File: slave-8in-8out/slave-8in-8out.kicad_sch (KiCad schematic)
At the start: 17 parts, among them J1 Conn_01x06_Male, J2 Screw_Terminal_01x02, J3 Conn_01x06_Female, J4 Screw_Terminal_01x04, J5 Screw_Terminal_01x04, J6 Screw_Terminal_01x04, J7 Screw_Terminal_01x04, J8 Conn_01x10_Male, J9 Screw_Terminal_01x02, SW1 SW_DIP_x03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

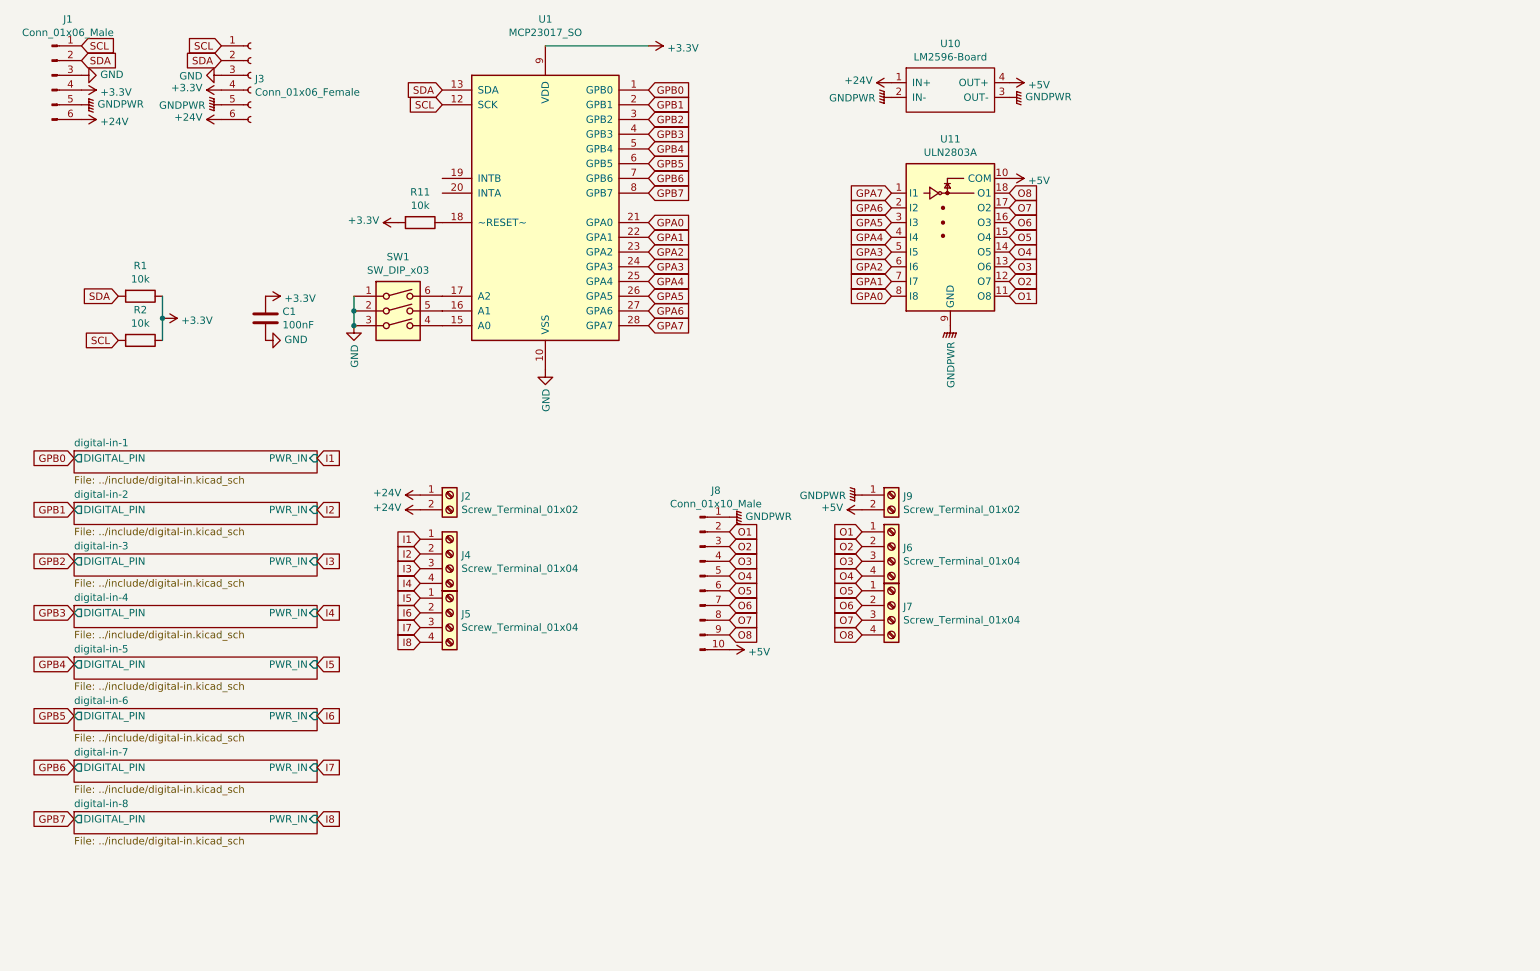
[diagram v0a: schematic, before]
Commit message: refactor 8in-8out
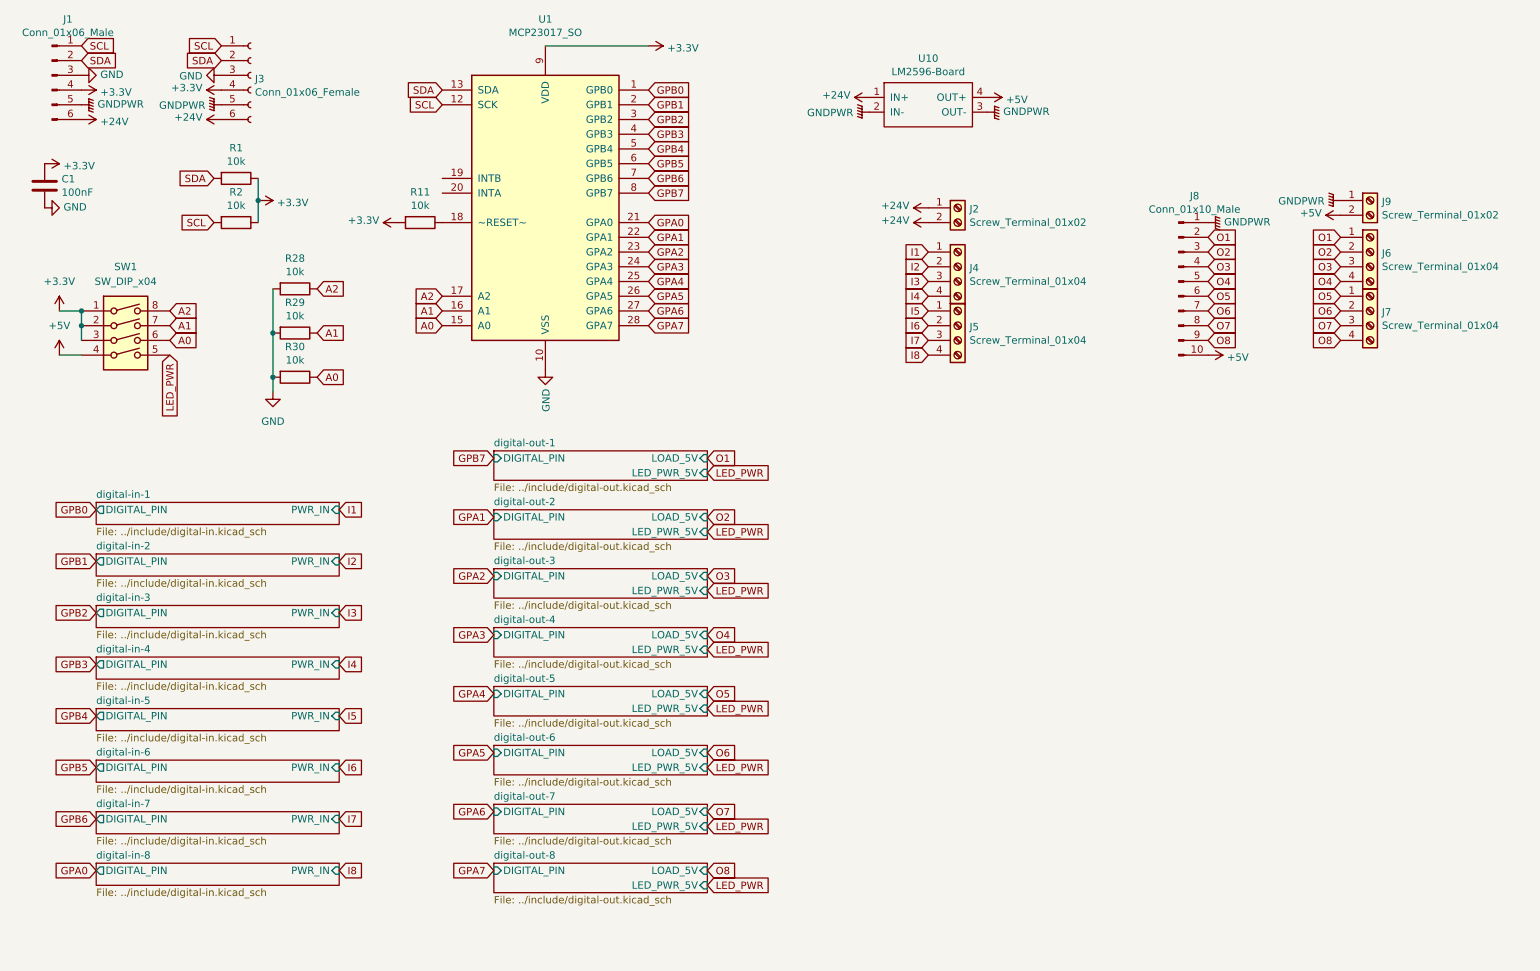
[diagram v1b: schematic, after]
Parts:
- removed SW1: SW_DIP_x03, Button_Switch_THT:SW_DIP_SPSTx03_Slide_9.78x9.8mm_W7.62mm_P2.54mm, symbol Switch:SW_DIP_x03
- removed U11: ULN2803A, Package_SO:SOIC-18W_7.5x11.6mm_P1.27mm, symbol Transistor_Array:ULN2803A
- added R28, R29, R30: 10k, Resistor_SMD:R_0402_1005Metric, symbol Device:R
- added SW1: SW_DIP_x04, Button_Switch_THT:SW_DIP_SPSTx04_Slide_9.78x12.34mm_W7.62mm_P2.54mm, symbol Switch:SW_DIP_x04
- R1, R11, R2: footprint Resistor_SMD:R_0805_2012Metric -> Resistor_SMD:R_0402_1005Metric; LCSC C17414 -> C25744
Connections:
- net +3V3: now also SW1.1, SW1.2, SW1.3
- net +5V: now also SW1.4
- net GND: now also R28.2, R29.2, R30.2
- net A0: now reaches U1.15 (A0)
- net A0: now also R30.1, SW1.6
- net A1: now reaches U1.16 (A1)
- net A1: now also R29.1, SW1.7
- net A2: now reaches U1.17 (A2)
- net A2: now also R28.1, SW1.8
- new net LED_PWR: SW1.5
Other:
- added sheet digital-out-1 (../include/digital-out.kicad_sch)
- added sheet digital-out-2 (../include/digital-out.kicad_sch)
- added sheet digital-out-3 (../include/digital-out.kicad_sch)
- added sheet digital-out-4 (../include/digital-out.kicad_sch)
- added sheet digital-out-5 (../include/digital-out.kicad_sch)
- added sheet digital-out-6 (../include/digital-out.kicad_sch)
- added sheet digital-out-7 (../include/digital-out.kicad_sch)
- added sheet digital-out-8 (../include/digital-out.kicad_sch)
- moved on the sheet: C1, J2, J4, J5, J6, J7, J8, J9, U10

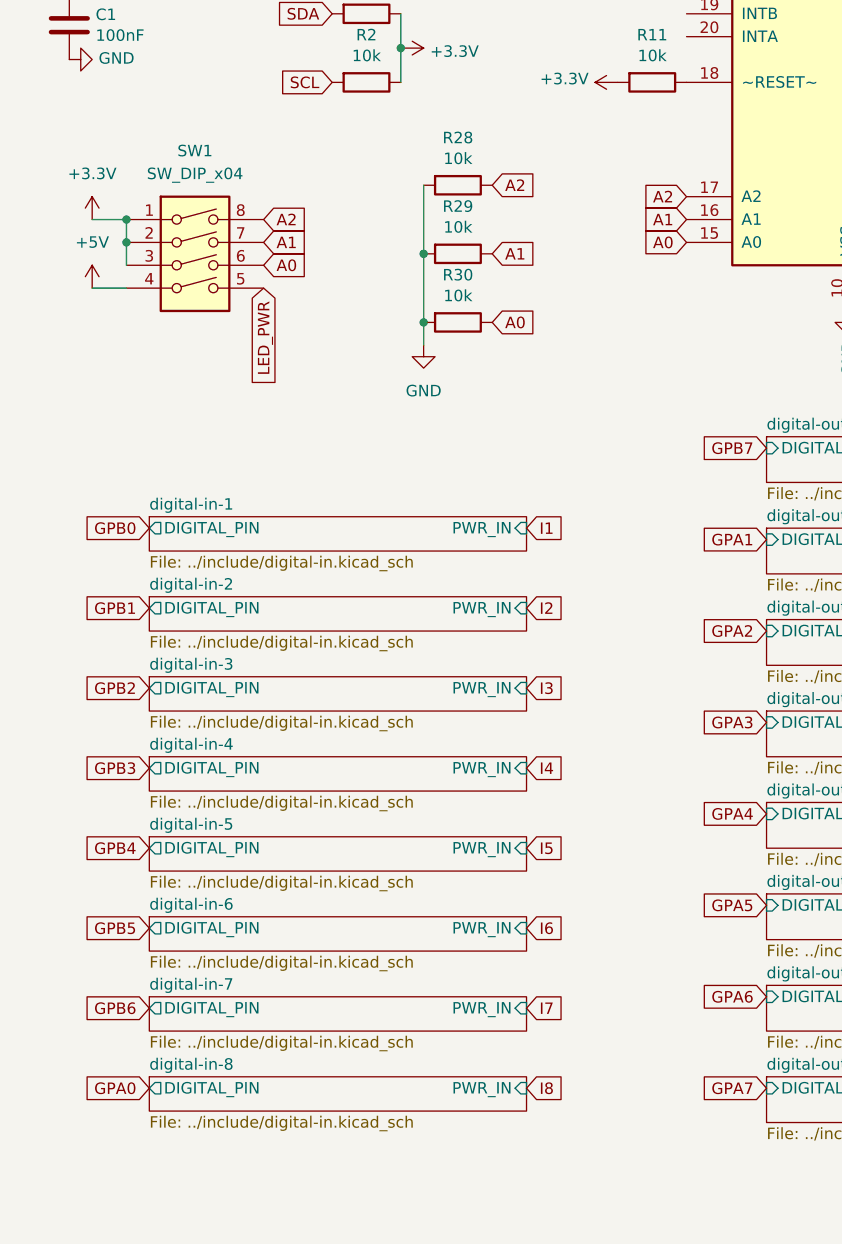
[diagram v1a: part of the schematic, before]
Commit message: refactor slave-8in-8out
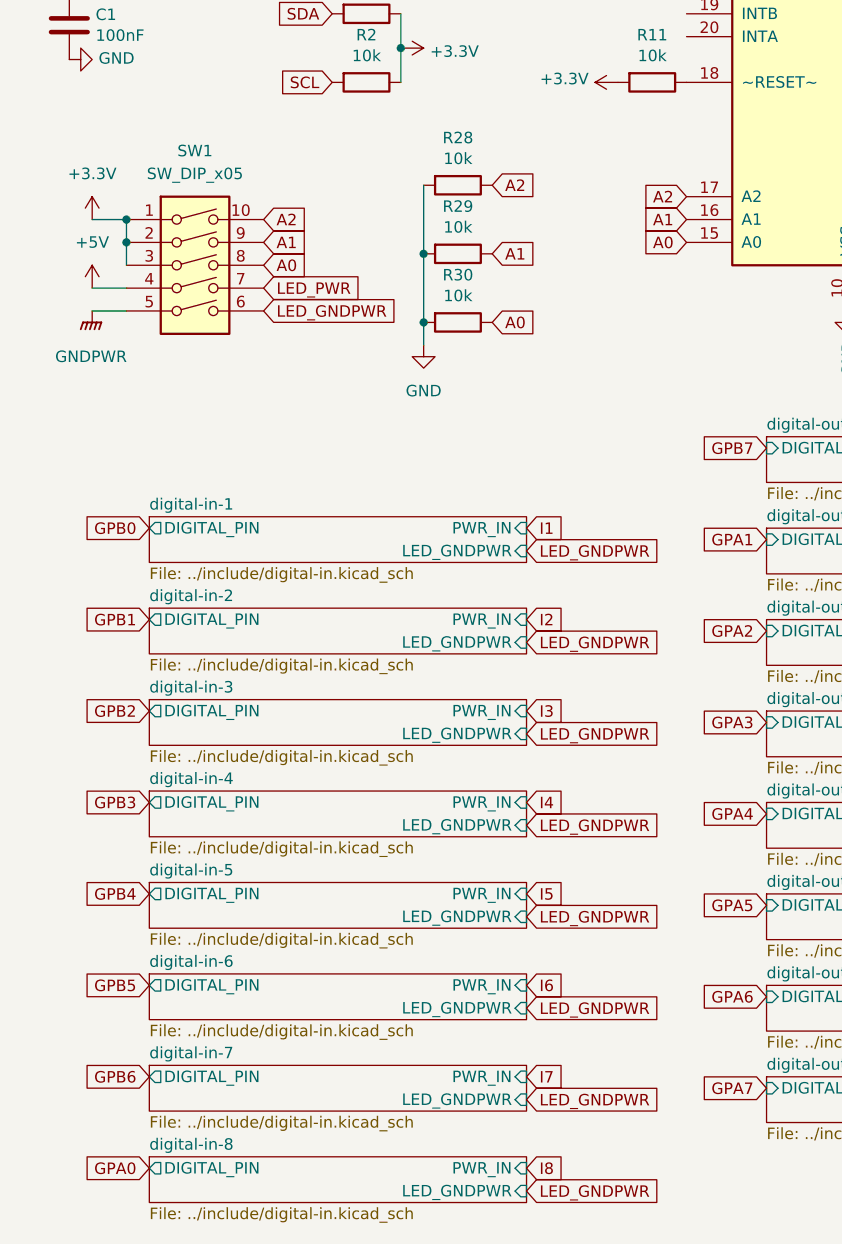
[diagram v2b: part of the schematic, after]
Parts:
- removed SW1: SW_DIP_x04, Button_Switch_THT:SW_DIP_SPSTx04_Slide_9.78x12.34mm_W7.62mm_P2.54mm, symbol Switch:SW_DIP_x04
- added SW1: SW_DIP_x05, Button_Switch_THT:SW_DIP_SPSTx05_Slide_9.78x14.88mm_W7.62mm_P2.54mm, symbol Switch:SW_DIP_x05
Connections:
- net +3V3: now also SW1.1, SW1.2, SW1.3
- net +5V: now also SW1.4
- net A0: now also SW1.8
- net A1: now also SW1.9
- net A2: now also SW1.10
- net GNDPWR: now also SW1.5
- net LED_PWR: now also SW1.7
- new net LED_GNDPWR: SW1.6
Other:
- sheet digital-in-1 ports: added LED_GNDPWR; removed none
- sheet digital-in-2 ports: added LED_GNDPWR; removed none
- sheet digital-in-3 ports: added LED_GNDPWR; removed none
- sheet digital-in-4 ports: added LED_GNDPWR; removed none
- sheet digital-in-5 ports: added LED_GNDPWR; removed none
- sheet digital-in-6 ports: added LED_GNDPWR; removed none
- sheet digital-in-7 ports: added LED_GNDPWR; removed none
- sheet digital-in-8 ports: added LED_GNDPWR; removed none

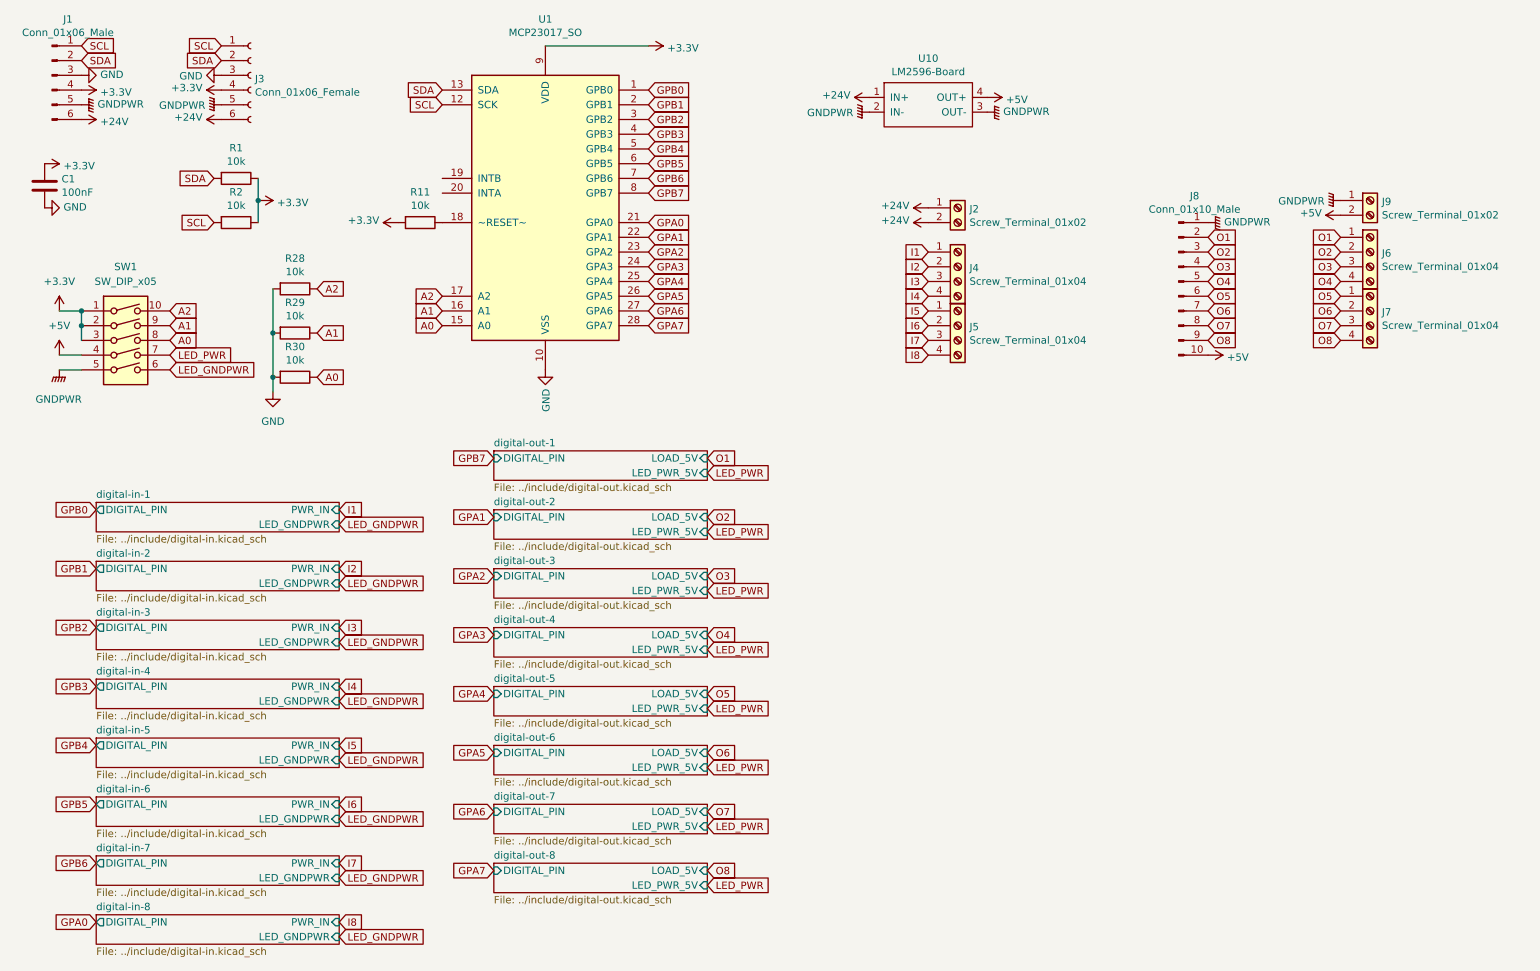
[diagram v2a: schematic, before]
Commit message: refactor slave-8in-8out
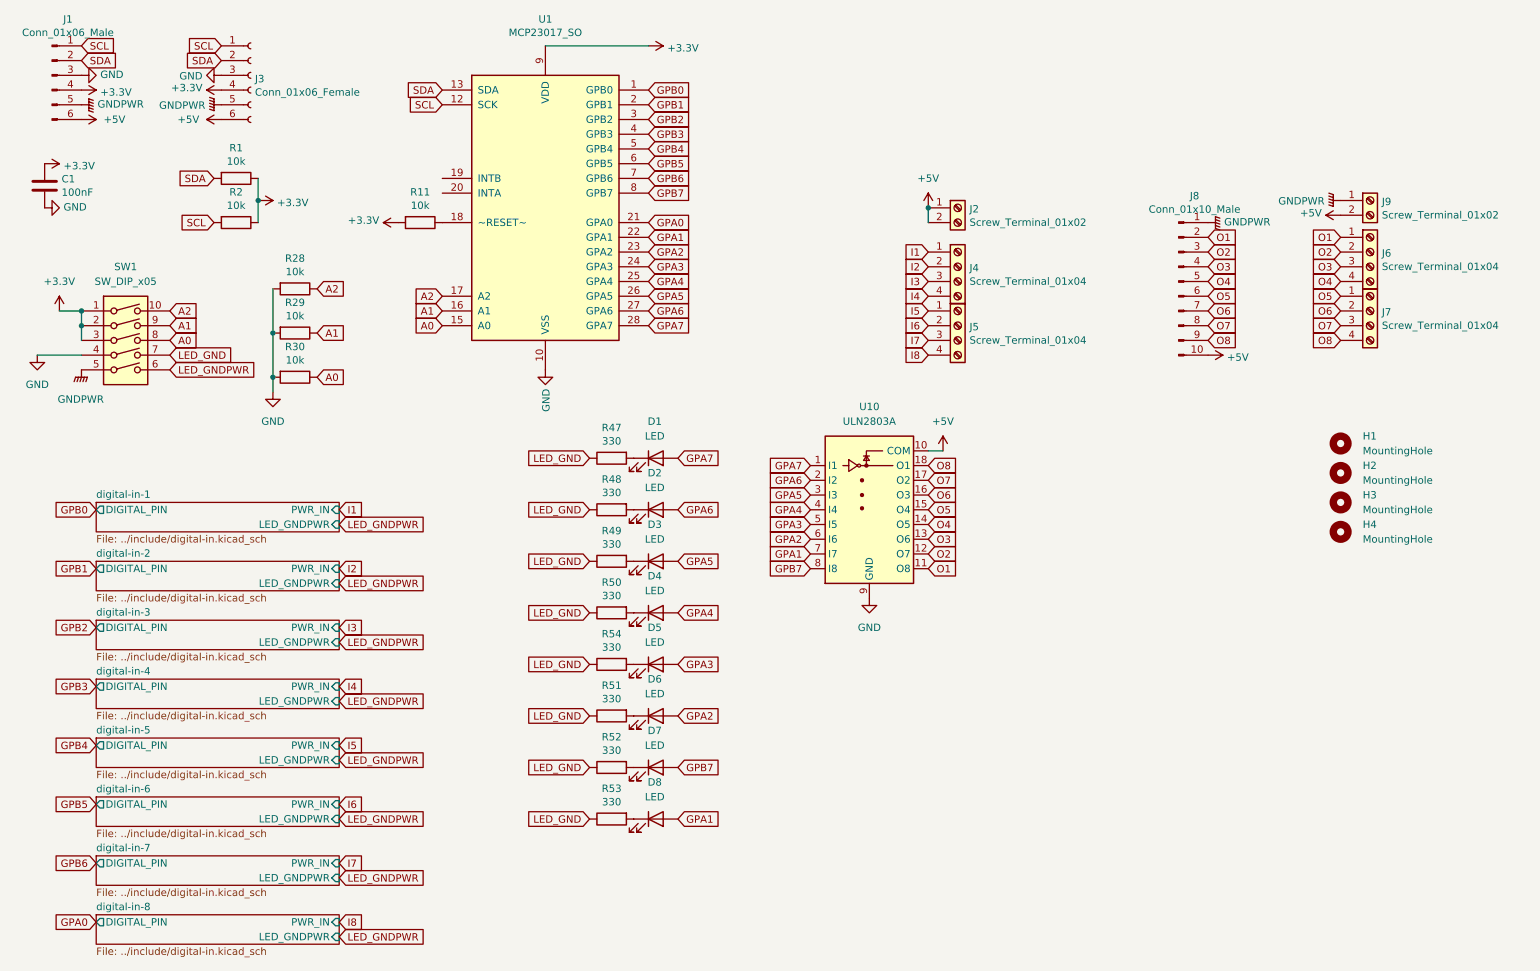
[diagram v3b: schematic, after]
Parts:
- removed U10: LM2596-Board, boards:LM2596-Board, symbol boards:LM2596-Board
- added D1, D2, D3, D4, D5, D6, D7, D8: LED, Resistor_SMD:R_0805_2012Metric, symbol Device:LED
- added H1, H2, H3, H4: MountingHole, MountingHole:MountingHole_3.2mm_M3, symbol Mechanical:MountingHole
- added R47, R48, R49, R50, R51, R52, R53, R54: 330, Resistor_SMD:R_0402_1005Metric, symbol Device:R
- added U10: ULN2803A, Package_SO:SOIC-18W_7.5x11.6mm_P1.27mm, symbol Transistor_Array:ULN2803A
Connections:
- net +24V is gone; now on net +5V: J1.6 (Pin_6), J2.1 (Pin_1), J2.2 (Pin_2), J3.6 (Pin_6)
- net +5V: now also U10.10 (COM); no longer SW1.4
- net GND: now also SW1.4, U10.9 (GND)
- net GPA1: now also D8.2 (A), U10.7 (I7)
- net GPA2: now also D6.2 (A), U10.6 (I6)
- net GPA3: now also D5.2 (A), U10.5 (I5)
- net GPA4: now also D4.2 (A), U10.4 (I4)
- net GPA5: now also D3.2 (A), U10.3 (I3)
- net GPA6: now also D2.2 (A), U10.2 (I2)
- net GPA7: now also D1.2 (A), U10.1 (I1)
- net GPB7: now also D7.2 (A), U10.8 (I8)
- net O1: now also U10.11 (O8)
- net O2: now also U10.12 (O7)
- net O3: now also U10.13 (O6)
- net O4: now also U10.14 (O5)
- net O5: now also U10.15 (O4)
- net O6: now also U10.16 (O3)
- net O7: now also U10.17 (O2)
- net O8: now also U10.18 (O1)
- net LED_PWR renamed LED_GND
- net LED_GND: now also R47.1, R48.1, R49.1, R50.1, R51.1, R52.1, R53.1, R54.1
- new net: D3.1 (K), R49.2
- new net: D1.1 (K), R47.2
- new net: D8.1 (K), R53.2
- new net: D2.1 (K), R48.2
- new net: D6.1 (K), R51.2
- new net: D5.1 (K), R54.2
- new net: D4.1 (K), R50.2
- new net: D7.1 (K), R52.2
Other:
- removed sheet digital-out-1
- removed sheet digital-out-2
- removed sheet digital-out-3
- removed sheet digital-out-4
- removed sheet digital-out-5
- removed sheet digital-out-6
- removed sheet digital-out-7
- removed sheet digital-out-8

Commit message: update slave-8in-8out pcb
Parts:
- U10: LCSC (none) -> C9683
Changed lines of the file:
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@@
+      (effects (font (size 1.27 1.27)) hide)
+    )
+    (property "LCSC" "C9683" (id 4) (at 163.83 99.06 0)
       (effects (font (size 1.27 1.27)) hide)
     )

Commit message: 8in-8out fab files
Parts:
- removed R11: 10k, Resistor_SMD:R_0402_1005Metric, symbol Device:R
- removed U1: MCP23017_SO, Package_SO:SOIC-28W_7.5x17.9mm_P1.27mm, symbol slave-8in-8out-rescue:MCP23017_SO-Interface_Expansion
- added U1: PCF8575, Package_SO:SSOP-24_5.3x8.2mm_P0.65mm, symbol custom:PCF8575
- H1, H2, H3, H4, SW1: LCSC (none) -> skip
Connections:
- net +3V3: now also U1.24 (VCC)
- net A0: now also U1.21 (A0)
- net A1: now also U1.2 (A1)
- net A2: now also U1.3 (A2)
- net GND: now also U1.12 (GND)
- net GPA0: now also D8.2 (A), U1.13 (P10)
- net GPA1: now also D7.2 (A), U1.14 (P11); no longer D8.2 (A)
- net GPA2: now also U1.15 (P12)
- net GPA3: now also U1.16 (P13)
- net GPA4: now also U1.17 (P14)
- net GPA5: now also U1.18 (P15)
- net GPA6: now also U1.19 (P16)
- net GPA7: now also U1.20 (P17)
- net GPB0: now also U1.4 (P00)
- net GPB1: now also U1.5 (P01)
- net GPB2: now also U1.6 (P02)
- net GPB3: now also U1.7 (P03)
- net GPB4: now also U1.8 (P04)
- net GPB5: now also U1.9 (P05)
- net GPB6: now also U1.10 (P06)
- net GPB7: now also U1.11 (P07); no longer D7.2 (A)
- net SCL: now also U1.22 (SCL)
- net SDA: now also U1.23 (SDA)
- no-connect marks 0 -> 1
